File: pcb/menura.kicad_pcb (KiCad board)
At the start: 2 copper layers, 123 x 97.2 mm, 56 parts

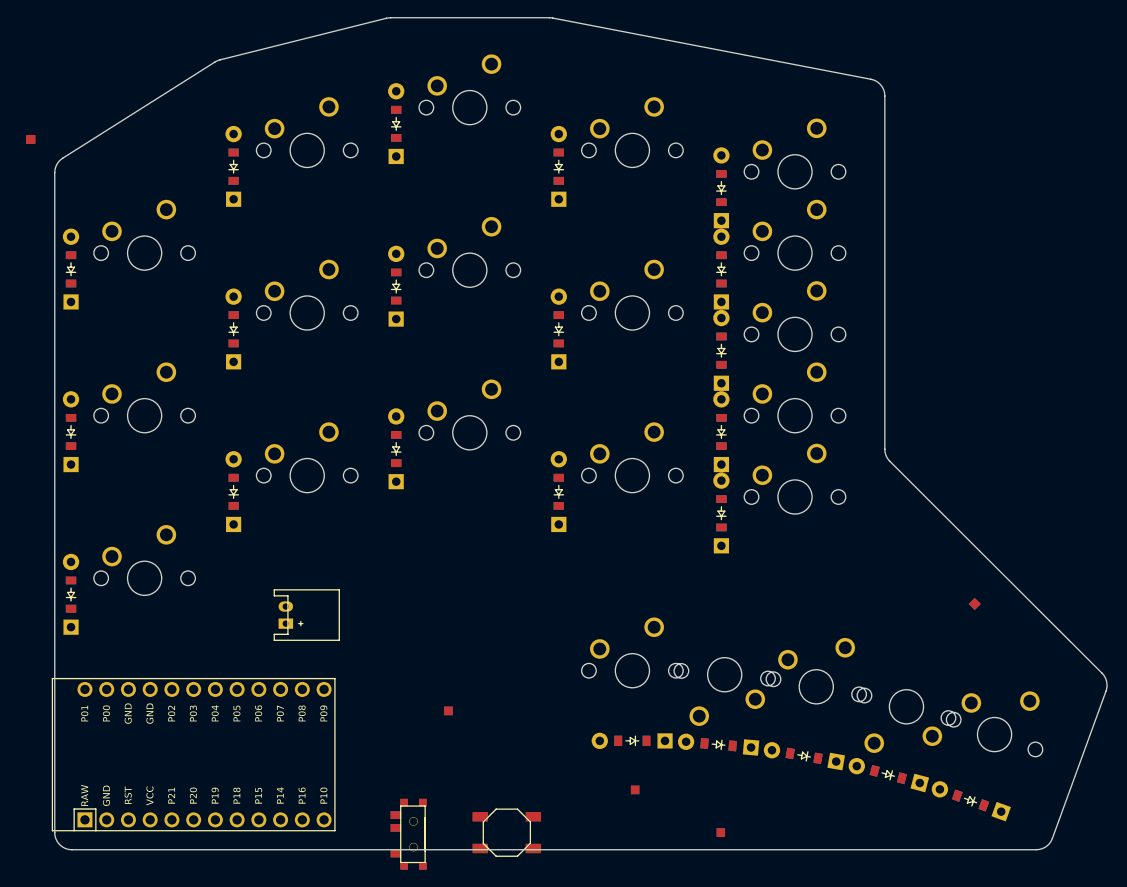
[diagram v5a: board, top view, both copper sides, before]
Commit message: add mounting holes
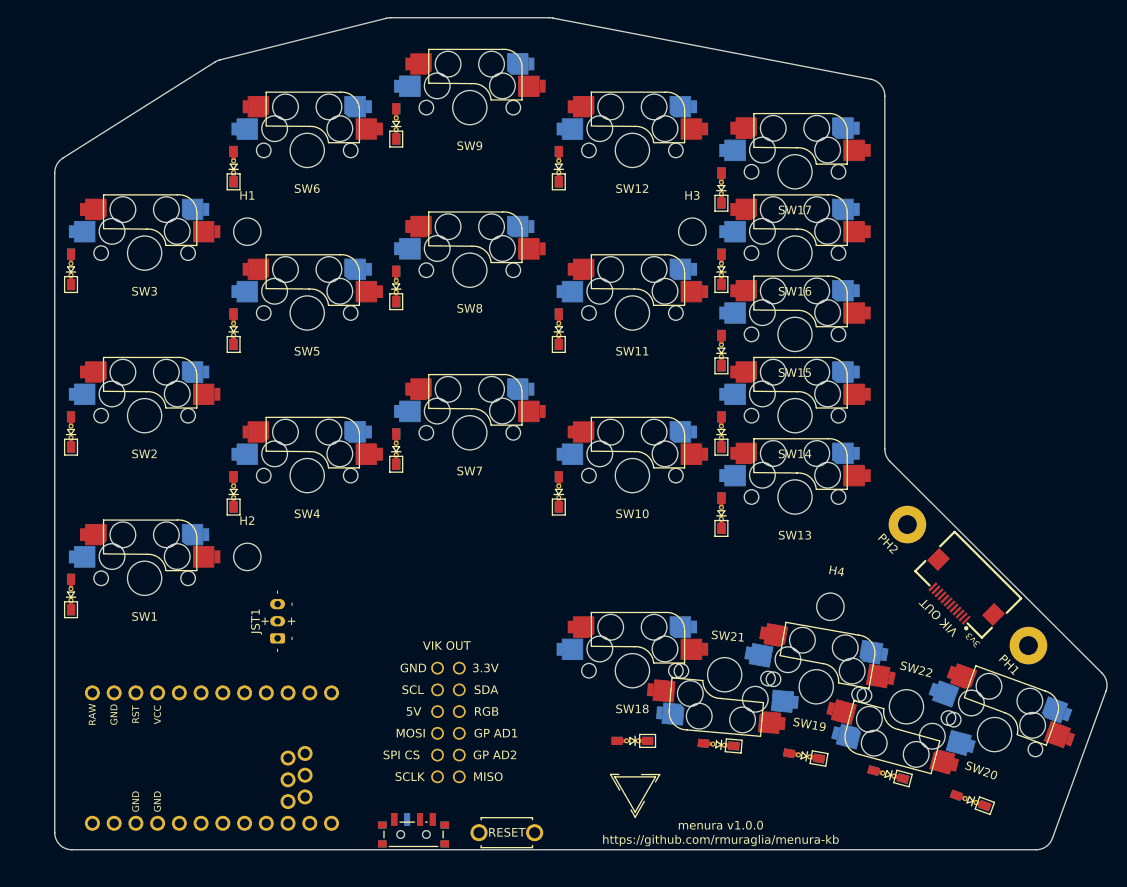
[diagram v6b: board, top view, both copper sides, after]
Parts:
- added H5: , SMDPad, F.Cu at (203.3, 107.9)
- added H6: , SMDPad, F.Cu at (189.1, 93.7)
- added PH1: MountingHole, MountingHole:MountingHole_2.2mm_M2_Pad, F.Cu at (203.3, 107.9)
- added PH2: MountingHole, MountingHole:MountingHole_2.2mm_M2_Pad, F.Cu at (189.1, 93.7)
- D1, D10, D11, D12, D13, D14, D15, D16, D17, D18, D19, D2, D20, D21, D22, D3, D4, D5, D6, D7, D8, D9: value (none) -> 1N4148W; footprint ComboDiode -> quappo:Diode_SMD-reversible-urchin
- H1, H2, H3, H4: value (none) -> MountingHole; footprint SMDPad -> MountingHole:MountingHole_3.2mm_M3
- JST1: value (none) -> Conn_01x03_Socket; footprint JST_PH_S2B-PH-K_02x2.00mm_Angled -> quappo:Connector_JST-PH-3prong
- LOGO1: value (none) -> menura; footprint SMDPad -> quappo:Logo_menura
- LOGO2: value (none) -> vik; footprint SMDPad -> quappo:Logo_vik-small
- MCU1: value (none) -> N!N; footprint ProMicro -> quappo:MCU_nice-nano
- PWR1: value (none) -> SW_SPDT; footprint E73:SPDT_C128955 -> quappo:Switch_power-reversible-kim
- RSW1: value (none) -> SW_Push; footprint E73:SW_TACT_ALPS_SKQGABE010 -> quappo:Switch_reset-2pin
- SW1, SW10, SW11, SW12, SW13, SW14, SW15, SW16, SW17, SW18, SW19, SW2, SW20, SW21, SW22, SW3, SW4, SW5, SW6, SW7, SW8, SW9: value (none) -> SW_Push; footprint MX -> quappo:Switch_MX-hotswap-reversible
- VIK1: value (none) -> ~; footprint SMDPad -> quappo:Connector_vik-keyboard-horizontal
- VIK2: value (none) -> ~; footprint SMDPad -> quappo:Connector_vik-keyboard-throughhole
- moved H4 108.2 mm to (180.1, 103.3), turned to -10 degrees
- moved H3 78.1 mm to (164.0, 59.5)
- moved H2 55.0 mm to (112.0, 97.5)
- moved H1 27.5 mm to (112.0, 59.5)
- moved VIK1 2.12 mm to (195.5, 101.5)
- moved JST1 1.66 mm to (118.0, 105.0)
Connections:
- D1 pad 1: (no net) -> row2
- D1 pad 2: (no net) -> Net-(D1-A)
- D10 pad 1: (no net) -> row2
- D10 pad 2: (no net) -> Net-(D10-A)
- D11 pad 1: (no net) -> row1
- D11 pad 2: (no net) -> Net-(D11-A)
- D12 pad 1: (no net) -> row0
- D12 pad 2: (no net) -> Net-(D12-A)
- D13 pad 1: (no net) -> row2
- D13 pad 2: (no net) -> Net-(D13-A)
- D14 pad 1: (no net) -> row1
- D14 pad 2: (no net) -> Net-(D14-A)
- D15 pad 1: (no net) -> row1
- D15 pad 2: (no net) -> Net-(D15-A)
- D16 pad 1: (no net) -> row0
- D16 pad 2: (no net) -> Net-(D16-A)
- D17 pad 1: (no net) -> row0
- D17 pad 2: (no net) -> Net-(D17-A)
- D18 pad 1: (no net) -> row3
- D18 pad 2: (no net) -> Net-(D18-A)
- D19 pad 1: (no net) -> row3
- D19 pad 2: (no net) -> Net-(D19-A)
- D2 pad 1: (no net) -> row1
- D2 pad 2: (no net) -> Net-(D2-A)
- D20 pad 1: (no net) -> row3
- D20 pad 2: (no net) -> Net-(D20-A)
- D21 pad 1: (no net) -> row3
- D21 pad 2: (no net) -> Net-(D21-A)
- D22 pad 1: (no net) -> row3
- D22 pad 2: (no net) -> Net-(D22-A)
- D3 pad 1: (no net) -> row0
- D3 pad 2: (no net) -> Net-(D3-A)
- D4 pad 1: (no net) -> row2
- D4 pad 2: (no net) -> Net-(D4-A)
- D5 pad 1: (no net) -> row1
- D5 pad 2: (no net) -> Net-(D5-A)
- D6 pad 1: (no net) -> row0
- D6 pad 2: (no net) -> Net-(D6-A)
- D7 pad 1: (no net) -> row2
- D7 pad 2: (no net) -> Net-(D7-A)
- D8 pad 1: (no net) -> row1
- D8 pad 2: (no net) -> Net-(D8-A)
- D9 pad 1: (no net) -> row0
- D9 pad 2: (no net) -> Net-(D9-A)
- JST1 pad 1: (no net) -> GND
- JST1 pad 2: (no net) -> Net-(JST1-Pin_2)
- MCU1 pad 1: RAW -> unconnected-(MCU1-006-Pad1)
- MCU1 pad 10: P14 -> CS
- MCU1 pad 11: P16 -> col4
- MCU1 pad 12: P10 -> row3
- MCU1 pad 13: P1 -> col3
- MCU1 pad 14: P0 -> col2
- MCU1 pad 15: GND -> col1
- MCU1 pad 16: GND -> col0
- MCU1 pad 17: P2 -> VIK_GPIO2
- MCU1 pad 18: P3 -> VIK_GPIO1
- MCU1 pad 19: P4 -> row2
- MCU1 pad 2: GND -> row0
- MCU1 pad 20: P5 -> row1
- MCU1 pad 21: P6 -> +3.3V
- MCU1 pad 22: P7 -> RST
- MCU1 pad 23: P8 -> GND
- MCU1 pad 24: P9 -> RAW
- MCU1 pad 3: RST -> GND
- MCU1 pad 4: VCC -> GND
- MCU1 pad 5: P21 -> SDA
- MCU1 pad 6: P20 -> SCL
- MCU1 pad 7: P19 -> SCLK
- MCU1 pad 8: P18 -> MISO
- MCU1 pad 9: P15 -> MOSI
- PWR1 pad 1: (no net) -> RAW
- PWR1 pad 2: (no net) -> Net-(JST1-Pin_2)
- PWR1 pad 3: (no net) -> unconnected-(PWR1-C-Pad3)
- RSW1 pad 1: (no net) -> GND
- RSW1 pad 2: (no net) -> RST
- SW1 pad 1: (no net) -> col0
- SW1 pad 2: (no net) -> Net-(D1-A)
- SW10 pad 1: (no net) -> col3
- SW10 pad 2: (no net) -> Net-(D10-A)
- SW11 pad 1: (no net) -> col3
- SW11 pad 2: (no net) -> Net-(D11-A)
- SW12 pad 1: (no net) -> col3
- SW12 pad 2: (no net) -> Net-(D12-A)
- SW13 pad 1: (no net) -> col4
- SW13 pad 2: (no net) -> Net-(D13-A)
- SW14 pad 1: (no net) -> col4
- SW14 pad 2: (no net) -> Net-(D14-A)
- SW15 pad 1: (no net) -> col4
- SW15 pad 2: (no net) -> Net-(D15-A)
- SW16 pad 1: (no net) -> col4
- SW16 pad 2: (no net) -> Net-(D16-A)
- SW17 pad 1: (no net) -> col4
- SW17 pad 2: (no net) -> Net-(D17-A)
- SW18 pad 1: (no net) -> col2
- SW18 pad 2: (no net) -> Net-(D18-A)
- SW19 pad 1: (no net) -> col3
- SW19 pad 2: (no net) -> Net-(D19-A)
- SW2 pad 1: (no net) -> col0
- SW2 pad 2: (no net) -> Net-(D2-A)
- SW20 pad 1: (no net) -> col4
- SW20 pad 2: (no net) -> Net-(D20-A)
- SW21 pad 1: (no net) -> col2
- SW21 pad 2: (no net) -> Net-(D21-A)
- SW22 pad 1: (no net) -> col3
- SW22 pad 2: (no net) -> Net-(D22-A)
- SW3 pad 1: (no net) -> col0
- SW3 pad 2: (no net) -> Net-(D3-A)
- SW4 pad 1: (no net) -> col1
- SW4 pad 2: (no net) -> Net-(D4-A)
- SW5 pad 1: (no net) -> col1
- SW5 pad 2: (no net) -> Net-(D5-A)
- SW6 pad 1: (no net) -> col1
- SW6 pad 2: (no net) -> Net-(D6-A)
- SW7 pad 1: (no net) -> col2
- SW7 pad 2: (no net) -> Net-(D7-A)
- SW8 pad 1: (no net) -> col2
- SW8 pad 2: (no net) -> Net-(D8-A)
- SW9 pad 1: (no net) -> col2
- SW9 pad 2: (no net) -> Net-(D9-A)
- VIK1 pad 1: (no net) -> +3.3V
- VIK2 pad 1: (no net) -> +3.3V
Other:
- net class Default removed

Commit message: one more pth
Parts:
- added H7: , SMDPad, F.Cu at (183.0, 42.0)
- added PH3: MountingHole, MountingHole:MountingHole_2.2mm_M2_Pad, F.Cu at (183.0, 42.0)
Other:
- outline, holes or cut-outs redrawn

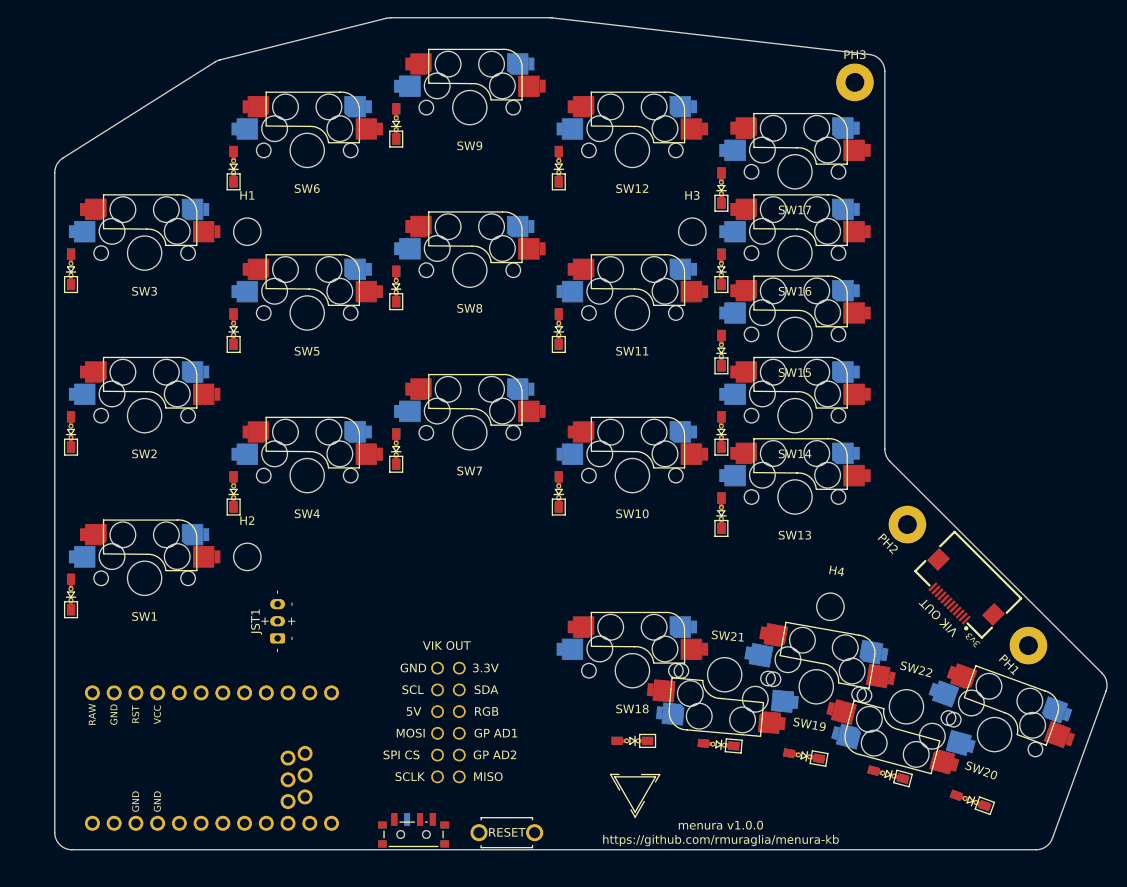
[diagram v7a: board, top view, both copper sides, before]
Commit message: remove plated holes on inner edge
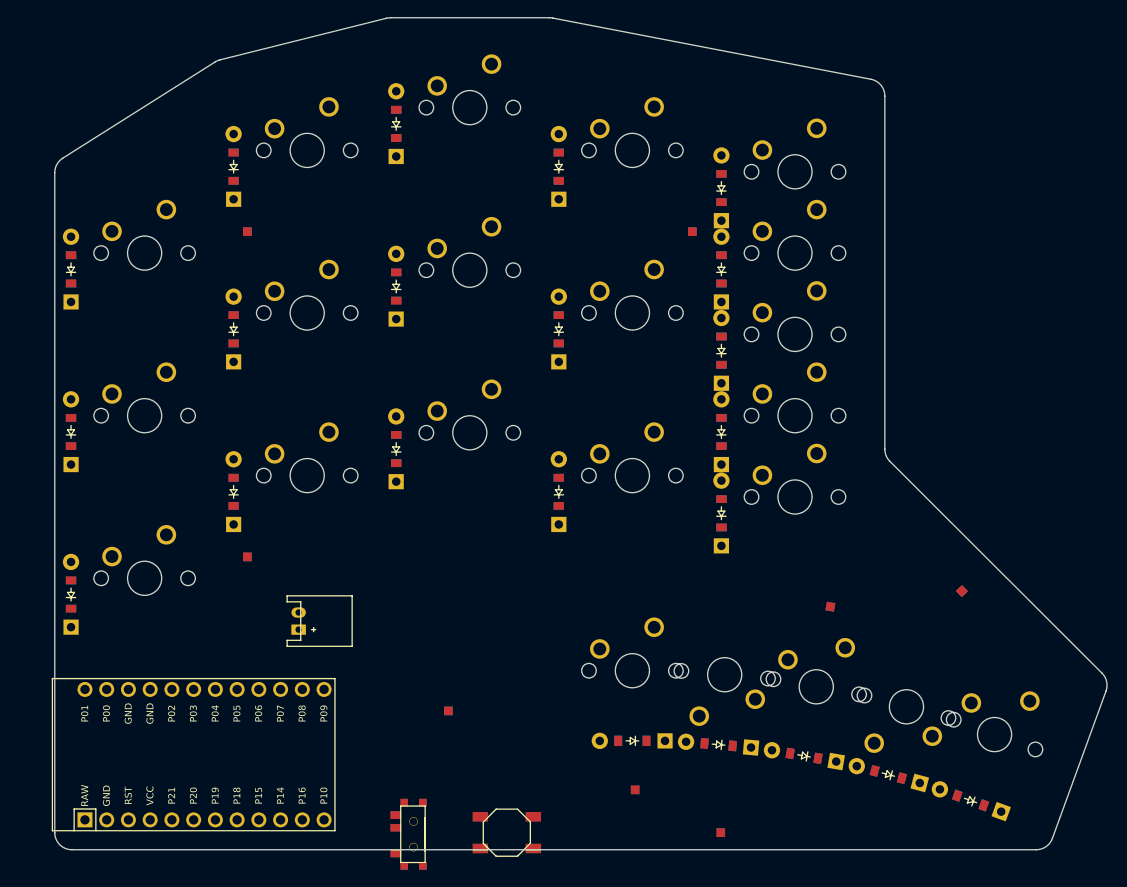
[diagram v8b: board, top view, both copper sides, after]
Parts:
- removed H5, H6, H7: , SMDPad
- removed PH1, PH2, PH3: MountingHole, MountingHole:MountingHole_2.2mm_M2_Pad
- D1, D10, D11, D12, D13, D14, D15, D16, D17, D18, D19, D2, D20, D21, D22, D3, D4, D5, D6, D7, D8, D9: value 1N4148W -> (none); footprint quappo:Diode_SMD-reversible-urchin -> ComboDiode
- H1, H2, H3, H4: value MountingHole -> (none); footprint MountingHole:MountingHole_3.2mm_M3 -> SMDPad
- JST1: value Conn_01x03_Socket -> (none); footprint quappo:Connector_JST-PH-3prong -> JST_PH_S2B-PH-K_02x2.00mm_Angled
- LOGO1: value menura -> (none); footprint quappo:Logo_menura -> SMDPad
- LOGO2: value vik -> (none); footprint quappo:Logo_vik-small -> SMDPad
- MCU1: value N!N -> (none); footprint quappo:MCU_nice-nano -> ProMicro
- PWR1: value SW_SPDT -> (none); footprint quappo:Switch_power-reversible-kim -> E73:SPDT_C128955
- RSW1: value SW_Push -> (none); footprint quappo:Switch_reset-2pin -> E73:SW_TACT_ALPS_SKQGABE010
- SW1, SW10, SW11, SW12, SW13, SW14, SW15, SW16, SW17, SW18, SW19, SW2, SW20, SW21, SW22, SW3, SW4, SW5, SW6, SW7, SW8, SW9: value SW_Push -> (none); footprint quappo:Switch_MX-hotswap-reversible -> MX
- VIK1: value ~ -> (none); footprint quappo:Connector_vik-keyboard-horizontal -> SMDPad
- VIK2: value ~ -> (none); footprint quappo:Connector_vik-keyboard-throughhole -> SMDPad
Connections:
- D1 pad 1: row2 -> (no net)
- D1 pad 2: Net-(D1-A) -> (no net)
- D10 pad 1: row2 -> (no net)
- D10 pad 2: Net-(D10-A) -> (no net)
- D11 pad 1: row1 -> (no net)
- D11 pad 2: Net-(D11-A) -> (no net)
- D12 pad 1: row0 -> (no net)
- D12 pad 2: Net-(D12-A) -> (no net)
- D13 pad 1: row2 -> (no net)
- D13 pad 2: Net-(D13-A) -> (no net)
- D14 pad 1: row1 -> (no net)
- D14 pad 2: Net-(D14-A) -> (no net)
- D15 pad 1: row1 -> (no net)
- D15 pad 2: Net-(D15-A) -> (no net)
- D16 pad 1: row0 -> (no net)
- D16 pad 2: Net-(D16-A) -> (no net)
- D17 pad 1: row0 -> (no net)
- D17 pad 2: Net-(D17-A) -> (no net)
- D18 pad 1: row3 -> (no net)
- D18 pad 2: Net-(D18-A) -> (no net)
- D19 pad 1: row3 -> (no net)
- D19 pad 2: Net-(D19-A) -> (no net)
- D2 pad 1: row1 -> (no net)
- D2 pad 2: Net-(D2-A) -> (no net)
- D20 pad 1: row3 -> (no net)
- D20 pad 2: Net-(D20-A) -> (no net)
- D21 pad 1: row3 -> (no net)
- D21 pad 2: Net-(D21-A) -> (no net)
- D22 pad 1: row3 -> (no net)
- D22 pad 2: Net-(D22-A) -> (no net)
- D3 pad 1: row0 -> (no net)
- D3 pad 2: Net-(D3-A) -> (no net)
- D4 pad 1: row2 -> (no net)
- D4 pad 2: Net-(D4-A) -> (no net)
- D5 pad 1: row1 -> (no net)
- D5 pad 2: Net-(D5-A) -> (no net)
- D6 pad 1: row0 -> (no net)
- D6 pad 2: Net-(D6-A) -> (no net)
- D7 pad 1: row2 -> (no net)
- D7 pad 2: Net-(D7-A) -> (no net)
- D8 pad 1: row1 -> (no net)
- D8 pad 2: Net-(D8-A) -> (no net)
- D9 pad 1: row0 -> (no net)
- D9 pad 2: Net-(D9-A) -> (no net)
- JST1 pad 1: GND -> (no net)
- JST1 pad 2: Net-(JST1-Pin_2) -> (no net)
- MCU1 pad 1: unconnected-(MCU1-006-Pad1) -> RAW
- MCU1 pad 10: CS -> P14
- MCU1 pad 11: col4 -> P16
- MCU1 pad 12: row3 -> P10
- MCU1 pad 13: col3 -> P1
- MCU1 pad 14: col2 -> P0
- MCU1 pad 15: col1 -> GND
- MCU1 pad 16: col0 -> GND
- MCU1 pad 17: VIK_GPIO2 -> P2
- MCU1 pad 18: VIK_GPIO1 -> P3
- MCU1 pad 19: row2 -> P4
- MCU1 pad 2: row0 -> GND
- MCU1 pad 20: row1 -> P5
- MCU1 pad 21: +3.3V -> P6
- MCU1 pad 22: RST -> P7
- MCU1 pad 23: GND -> P8
- MCU1 pad 24: RAW -> P9
- MCU1 pad 3: GND -> RST
- MCU1 pad 4: GND -> VCC
- MCU1 pad 5: SDA -> P21
- MCU1 pad 6: SCL -> P20
- MCU1 pad 7: SCLK -> P19
- MCU1 pad 8: MISO -> P18
- MCU1 pad 9: MOSI -> P15
- PWR1 pad 1: RAW -> (no net)
- PWR1 pad 2: Net-(JST1-Pin_2) -> (no net)
- PWR1 pad 3: unconnected-(PWR1-C-Pad3) -> (no net)
- RSW1 pad 1: GND -> (no net)
- RSW1 pad 2: RST -> (no net)
- SW1 pad 1: col0 -> (no net)
- SW1 pad 2: Net-(D1-A) -> (no net)
- SW10 pad 1: col3 -> (no net)
- SW10 pad 2: Net-(D10-A) -> (no net)
- SW11 pad 1: col3 -> (no net)
- SW11 pad 2: Net-(D11-A) -> (no net)
- SW12 pad 1: col3 -> (no net)
- SW12 pad 2: Net-(D12-A) -> (no net)
- SW13 pad 1: col4 -> (no net)
- SW13 pad 2: Net-(D13-A) -> (no net)
- SW14 pad 1: col4 -> (no net)
- SW14 pad 2: Net-(D14-A) -> (no net)
- SW15 pad 1: col4 -> (no net)
- SW15 pad 2: Net-(D15-A) -> (no net)
- SW16 pad 1: col4 -> (no net)
- SW16 pad 2: Net-(D16-A) -> (no net)
- SW17 pad 1: col4 -> (no net)
- SW17 pad 2: Net-(D17-A) -> (no net)
- SW18 pad 1: col2 -> (no net)
- SW18 pad 2: Net-(D18-A) -> (no net)
- SW19 pad 1: col3 -> (no net)
- SW19 pad 2: Net-(D19-A) -> (no net)
- SW2 pad 1: col0 -> (no net)
- SW2 pad 2: Net-(D2-A) -> (no net)
- SW20 pad 1: col4 -> (no net)
- SW20 pad 2: Net-(D20-A) -> (no net)
- SW21 pad 1: col2 -> (no net)
- SW21 pad 2: Net-(D21-A) -> (no net)
- SW22 pad 1: col3 -> (no net)
- SW22 pad 2: Net-(D22-A) -> (no net)
- SW3 pad 1: col0 -> (no net)
- SW3 pad 2: Net-(D3-A) -> (no net)
- SW4 pad 1: col1 -> (no net)
- SW4 pad 2: Net-(D4-A) -> (no net)
- SW5 pad 1: col1 -> (no net)
- SW5 pad 2: Net-(D5-A) -> (no net)
- SW6 pad 1: col1 -> (no net)
- SW6 pad 2: Net-(D6-A) -> (no net)
- SW7 pad 1: col2 -> (no net)
- SW7 pad 2: Net-(D7-A) -> (no net)
- SW8 pad 1: col2 -> (no net)
- SW8 pad 2: Net-(D8-A) -> (no net)
- SW9 pad 1: col2 -> (no net)
- SW9 pad 2: Net-(D9-A) -> (no net)
- VIK1 pad 1: +3.3V -> (no net)
- VIK2 pad 1: +3.3V -> (no net)
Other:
- outline, holes or cut-outs redrawn
- net class Default added: clearance 0.2, trace_width 0.25, via_dia 0.8, via_drill 0.4
